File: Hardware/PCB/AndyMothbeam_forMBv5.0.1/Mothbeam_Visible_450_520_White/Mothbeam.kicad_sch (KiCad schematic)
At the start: 26 parts, among them CN1 X6511FRS-04-C85D30, SW2 SW_DIP_x04, U1 BCR421U, U2 BCR421U, U3 BCR421U, U4 M3535N1UVS8U12- 405NM, U5 M3535N1UVS8U06-385NM, U6 JNJ-LEHG0113W120/45MIL/525-53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

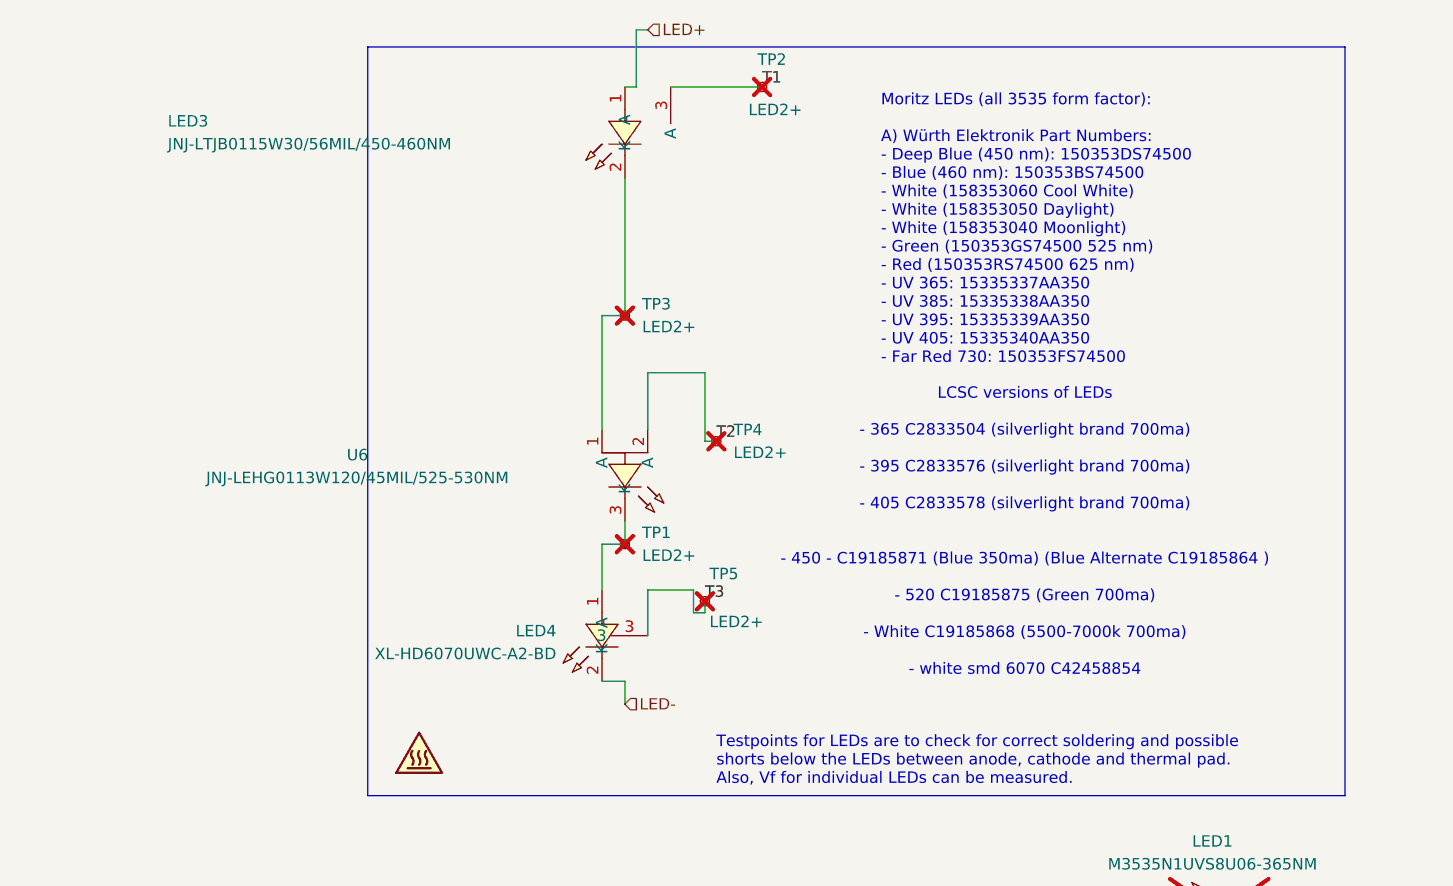
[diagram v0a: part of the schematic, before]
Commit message: Created 3535 Mothbeams for UV and V
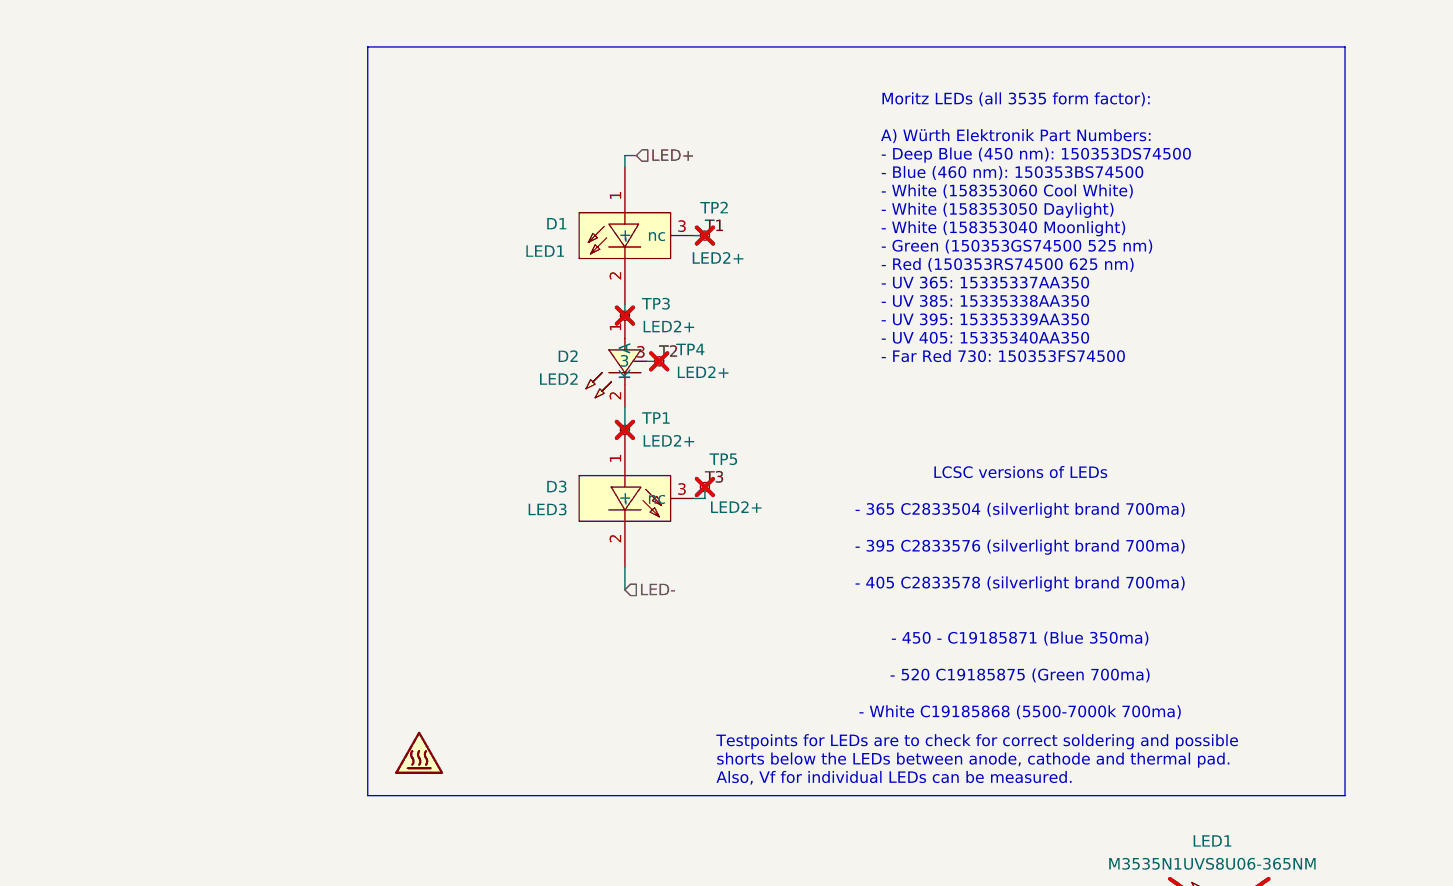
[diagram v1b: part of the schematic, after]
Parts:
- removed LED3: JNJ-LTJB0115W30/56MIL/450-460NM, easyeda2kicad:LED-SMD_3P-L3.5-W3.5-FD-1, symbol easyeda2kicad:JNJ-LTJB0115W30_56MIL_450-460NM
- removed LED4: XL-HD6070UWC-A2-BD, easyeda2kicad:LED-SMD_XL-HD6070UBC-A2, symbol easyeda2kicad:XL-HD6070UWC-A2-BD
- removed U6: JNJ-LEHG0113W120/45MIL/525-530NM, easyeda2kicad:LED-SMD_3P-L3.5-W3.5-R-RD_C9900043159, symbol easyeda2kicad:JNJ-LEHG0113W120_45MIL_525-530NM
- added D1: LED1, easyeda2kicad:LED-SMD_3P-L3.5-W3.5-R-RD-C, symbol easyeda2kicad:M3535N1UVS8U12-365NM
- added D2: LED2, easyeda2kicad:LED-SMD_3P-L3.5-W3.5-R-RD-C, symbol easyeda2kicad:M3535N1UVS8U12-395NM
- added D3: LED3, easyeda2kicad:LED-SMD_3P-L3.5-W3.5-R-RD-C, symbol easyeda2kicad:M3535N1UVS8U12-405NM
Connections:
- net LED+: now also D1.1 (+)
- net LED-: now also D3.2 (-)
- net T1: now also D1.3 (nc)
- net T2: now also D2.3
- net T3: now also D3.3 (nc)
- net at TP3.1: now also D1.2 (-), D2.1 (A)
- net at TP1.1: now also D2.2 (K), D3.1 (+)
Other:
- note added: "LCSC versions of LEDs - 365 C2833504 (silverlight brand 700ma) - 395 C2833576 (silverlight brand 700ma) - 405 C2833578 (silverlight brand 700ma) - 450 - C19185871 (Blue 350ma) - 520 C19185875 (Green 700ma) - White C19185868 (5500-7000k 700ma)"
- note removed: "LCSC versions of LEDs - 365 C2833504 (silverlight brand 700ma) - 395 C2833576 (silverlight brand 700ma) - 405 C2833578 (silverlight brand 700ma) - 450 - C19185871 (Blue 350ma) (Blue Alternate C19185864 ) - 520 C19185875 (Green 700ma) - White C19185868 (5500-7000k 700ma) - white smd 6070 C42458854"
- moved on the sheet: TP1, TP2, TP4, TP5

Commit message: before changing footprints on Visible board
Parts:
- removed D1: LED1, easyeda2kicad:LED-SMD_3P-L3.5-W3.5-R-RD-C, symbol easyeda2kicad:M3535N1UVS8U12-365NM
- removed D2: LED2, easyeda2kicad:LED-SMD_3P-L3.5-W3.5-R-RD-C, symbol easyeda2kicad:M3535N1UVS8U12-395NM
- removed D3: LED3, easyeda2kicad:LED-SMD_3P-L3.5-W3.5-R-RD-C, symbol easyeda2kicad:M3535N1UVS8U12-405NM
- added LED2: JNJ-LEJB0111W60/26MIL/450-460NM, easyeda2kicad:LED-SMD_3P-L3.5-W3.5_JNJ-LEJB0111W60, symbol easyeda2kicad:JNJ-LEJB0111W60_26MIL_450-460NM
- added LED3: JNJ-LEJW0113W30/C36MIL/5500-6500K, easyeda2kicad:LED-SMD_3P-L3.5-W3.5-R-RD-B, symbol easyeda2kicad:JNJ-LEJW0113W30_C36MIL_5500-6500K
- added U6: JNJ-LEHG0113W120/45MIL/525-530NM, easyeda2kicad:LED-SMD_3P-L3.5-W3.5-R-RD_C9900043159, symbol easyeda2kicad:JNJ-LEHG0113W120_45MIL_525-530NM
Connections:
- net LED+: now also LED2.3 (A)
- net LED-: now also LED3.3
- net T1: now also LED2.2 (K)
- net T2: now also U6.2 (A)
- net T3: now also LED3.2
- net at TP3.1: now also LED2.1 (K), U6.1 (A)
- net at TP1.1: now also LED3.1, U6.3 (K)
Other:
- moved on the sheet: TP1, TP2, TP4, TP5

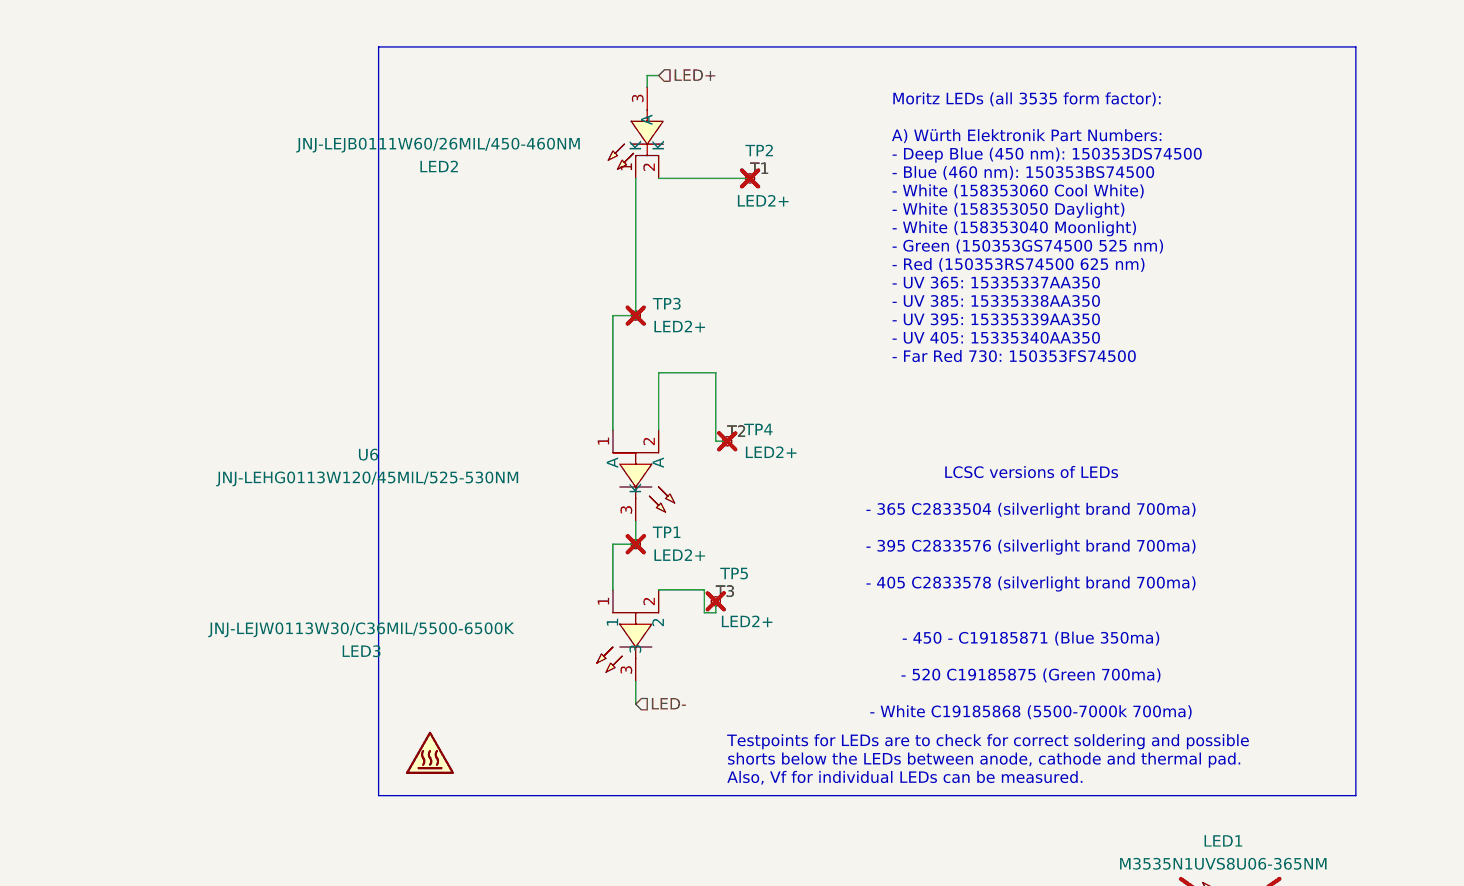
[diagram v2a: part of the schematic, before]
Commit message: new substitute parts
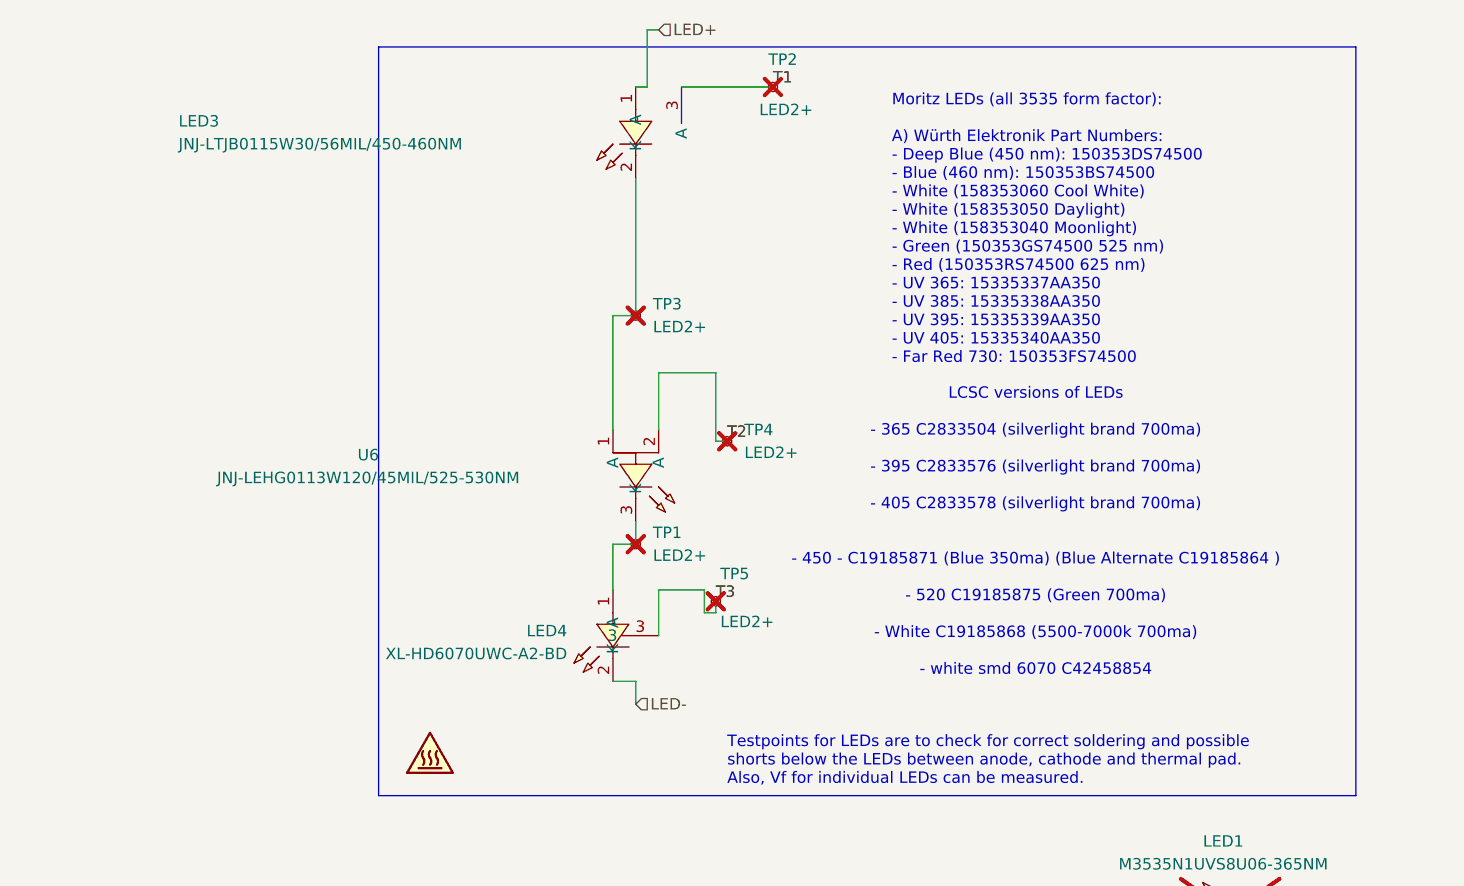
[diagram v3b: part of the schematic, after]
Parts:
- removed LED2: JNJ-LEJB0111W60/26MIL/450-460NM, easyeda2kicad:LED-SMD_3P-L3.5-W3.5_JNJ-LEJB0111W60, symbol easyeda2kicad:JNJ-LEJB0111W60_26MIL_450-460NM
- removed LED3: JNJ-LEJW0113W30/C36MIL/5500-6500K, easyeda2kicad:LED-SMD_3P-L3.5-W3.5-R-RD-B, symbol easyeda2kicad:JNJ-LEJW0113W30_C36MIL_5500-6500K
- added LED3: JNJ-LTJB0115W30/56MIL/450-460NM, easyeda2kicad:LED-SMD_3P-L3.5-W3.5-FD-1, symbol easyeda2kicad:JNJ-LTJB0115W30_56MIL_450-460NM
- added LED4: XL-HD6070UWC-A2-BD, easyeda2kicad:LED-SMD_XL-HD6070UBC-A2, symbol easyeda2kicad:XL-HD6070UWC-A2-BD
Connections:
- net LED+: now also LED3.1 (A)
- net LED-: now also LED4.2 (K)
- net T1: now also LED3.3 (A)
- net T3: now also LED4.3
- net at TP1.1, U6.3 (K): now also LED4.1 (A)
- net at TP3.1, U6.1 (A): now also LED3.2 (K)
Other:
- note added: "LCSC versions of LEDs - 365 C2833504 (silverlight brand 700ma) - 395 C2833576 (silverlight brand 700ma) - 405 C2833578 (silverlight brand 700ma) - 450 - C19185871 (Blue 350ma) (Blue Alternate C19185864 ) - 520 C19185875 (Green 700ma) - White C19185868 (5500-7000k 700ma) - white smd 6070 C42458854"
- note removed: "LCSC versions of LEDs - 365 C2833504 (silverlight brand 700ma) - 395 C2833576 (silverlight brand 700ma) - 405 C2833578 (silverlight brand 700ma) - 450 - C19185871 (Blue 350ma) - 520 C19185875 (Green 700ma) - White C19185868 (5500-7000k 700ma)"
- moved on the sheet: TP2
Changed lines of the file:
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@@
 		)
 	)
-	(text "LCSC versions of LEDs\n\n- 365 C2833504 (silverlight brand 700ma)\n\n- 395 C2833576 (silverlight brand 700ma)\n\n- 405 C2833578 (silverlight brand 700ma)\n\n\n- 450 - C19185871 (Blue 350ma)\n\n- 520 C19185875 (Green 700ma)\n\n- White C19185868 (5500-7000k 700ma)"
+	(text "LCSC versions of LEDs\n\n- 365 C2833504 (silverlight brand 700ma)\n\n- 395 C2833576 (silverlight brand 700ma)\n\n- 405 C2833578 (silverlight brand 700ma)\n\n\n- 450 - C19185871 (Blue 350ma) (Blue Alternate C19185864 )\n\n- 520 C19185875 (Green 700ma)\n\n- White C19185868 (5500-7000k 700ma)\n\n- white smd 6070 C42458854"
 		(exclude_from_sim no)
-		(at 245.872 76.708 0)
+		(at 246.38 69.85 0)
 		(effects
 			(font
@@
 	(wire
 		(pts
+			(xy 204.47 76.2) (xy 204.47 81.28)
+		)
+		(stroke
+			(width 0)
+			(type default)
+		)
+	)
+	(wire
+		(pts
 			(xy 45.72 134.62) (xy 48.26 134.62)
 		)
@@
 	(wire
 		(pts
+			(xy 203.2 13.97) (xy 203.2 20.32)
+		)
+		(stroke
+			(width 0)
+			(type default)
+		)
+	)
+	(wire
+		(pts
 			(xy 210.82 78.74) (xy 210.82 77.47)
 		)
@@
 	(wire
 		(pts
+			(xy 203.2 20.32) (xy 201.93 20.32)
+		)
+		(stroke
+			(width 0)
+			(type default)
+		)
+	)
+	(wire
+		(pts
 			(xy 201.93 30.48) (xy 201.93 45.72)
 		)
@@
 	(wire
 		(pts
+			(xy 199.39 86.36) (xy 201.93 86.36)
+		)
+		(stroke
+			(width 0)
+			(type default)
+		)
+	)
+	(wire
+		(pts
 			(xy 170.18 138.43) (xy 175.26 138.43)
 		)
@@
 	(wire
 		(pts
-			(xy 204.47 30.48) (xy 214.63 30.48)
+			(xy 207.01 20.32) (xy 217.17 20.32)
 		)
 		(stroke
@@
 	(wire
 		(pts
-			(xy 203.2 20.32) (xy 203.2 19.05)
-		)
-		(stroke
-			(width 0)
-			(type default)
-		)
-	)
-	(wire
-		(pts
 			(xy 41.91 134.62) (xy 41.91 127)
 		)
@@
 	(wire
 		(pts
-			(xy 203.2 19.05) (xy 204.47 19.05)
+			(xy 203.2 13.97) (xy 204.47 13.97)
 		)
 		(stroke
@@
 	)
 	(label "T1"
-		(at 214.63 30.48 0)
+		(at 217.17 20.32 0)
 		(effects
 			(font
@@
 	(hierarchical_label "LED+"
 		(shape input)
-		(at 204.47 19.05 0)
+		(at 204.47 13.97 0)
 		(effects
 			(font
@@
 	(symbol
 		(lib_id "Connector:TestPoint_Small")
-		(at 214.63 30.48 0)
+		(at 217.17 20.32 0)
 		(unit 1)
 		(exclude_from_sim no)
@@
 		(dnp yes)
 		(property "Reference" "TP2"
-			(at 214.122 27.432 0)
+			(at 216.662 17.272 0)
 			(effects
 				(font
@@
 		)
 		(property "Value" "LED2+"
-			(at 213.106 33.02 0)
+			(at 215.646 22.86 0)
 			(effects
 				(font
@@
 		)
 		(property "Footprint" "TestPoint:TestPoint_Pad_D1.5mm"
-			(at 219.71 30.48 0)
+			(at 222.25 20.32 0)
 			(effects
 				(font
@@
 		)
 		(property "Datasheet" "~"
-			(at 219.71 30.48 0)
+			(at 222.25 20.32 0)
 			(effects
 				(font
@@
 		)
 		(property "Description" ""
-			(at 214.63 30.48 0)
+			(at 217.17 20.32 0)
 			(effects
 				(font
@@
 	)
 	(symbol
-		(lib_id "easyeda2kicad:JNJ-LEJW0113W30_C36MIL_5500-6500K")
-		(at 201.93 81.28 90)
-		(unit 1)
-		(exclude_from_sim no)
-		(in_bom yes)
-		(on_board yes)
-		(dnp no)
-		(property "Reference" "LED3"
-			(at 171.45 83.058 90)
-			(effects
-				(font
-					(size 1.27 1.27)
-				)
-			)
-		)
-		(property "Value" "JNJ-LEJW0113W30/C36MIL/5500-6500K"
-			(at 171.45 80.518 90)
-			(effects
-				(font
-					(size 1.27 1.27)
-				)
-			)
-		)
-		(property "Footprint" "easyeda2kicad:LED-SMD_3P-L3.5-W3.5-R-RD-B"
-			(at 212.09 81.28 0)
-			(effects
-				(font
-					(size 1.27 1.27)
-				)
-				(hide yes)
-			)
-		)
-		(property "Datasheet" ""
-			(at 201.93 81.28 0)
-			(effects
-				(font
-					(size 1.27 1.27)
-				)
-				(hide yes)
-			)
-		)
-		(property "Description" ""
-			(at 201.93 81.28 0)
-			(effects
-				(font
-					(size 1.27 1.27)
-				)
-				(hide yes)
-			)
-		)
-		(property "LCSC Part" "C19185868"
-			(at 214.63 81.28 0)
-			(effects
-				(font
-					(size 1.27 1.27)
-				)
-				(hide yes)
-			)
-		)
-		(pin "1"
-		)
-		(pin "3"
-		)
-		(pin "2"
-		)
-		(instances
-			(project ""
-				(path "/a270892a-30ca-43aa-91d1-ed114756b159"
-					(reference "LED3")
-					(unit 1)
-				)
-			)
-		)
-	)
-	(symbol
 		(lib_id "Mechanical:Fiducial")
 		(at 27.94 183.515 0)
@@
 	)
 	(symbol
-		(lib_id "easyeda2kicad:JNJ-LEJB0111W60_26MIL_450-460NM")
-		(at 203.2 25.4 90)
-		(unit 1)
-		(exclude_from_sim no)
-		(in_bom yes)
-		(on_board yes)
-		(dnp no)
-		(property "Reference" "LED2"
-			(at 180.086 29.21 90)
-			(effects
-				(font
-					(size 1.27 1.27)
-				)
-			)
-		)
-		(property "Value" "JNJ-LEJB0111W60/26MIL/450-460NM"
-			(at 180.086 26.67 90)
-			(effects
-				(font
-					(size 1.27 1.27)
-				)
-			)
-		)
-		(property "Footprint" "easyeda2kicad:LED-SMD_3P-L3.5-W3.5_JNJ-LEJB0111W60"
-			(at 212.09 25.4 0)
-			(effects
-				(font
-					(size 1.27 1.27)
-				)
-				(hide yes)
-			)
-		)
-		(property "Datasheet" ""
-			(at 203.2 25.4 0)
-			(effects
-				(font
-					(size 1.27 1.27)
-				)
-				(hide yes)
-			)
-		)
-		(property "Description" ""
-			(at 203.2 25.4 0)
-			(effects
-				(font
-					(size 1.27 1.27)
-				)
-				(hide yes)
-			)
-		)
-		(property "LCSC Part" "C19185871"
-			(at 214.63 25.4 0)
-			(effects
-				(font
-					(size 1.27 1.27)
-				)
-				(hide yes)
-			)
-		)
-		(pin "2"
-		)
-		(pin "1"
-		)
-		(pin "3"
-		)
-		(instances
-			(project ""
-				(path "/a270892a-30ca-43aa-91d1-ed114756b159"
-					(reference "LED2")
-					(unit 1)
-				)
-			)
-		)
-	)
-	(symbol
 		(lib_id "easyeda2kicad:BCR421UW6-7")
 		(at 60.96 134.62 180)
@@
 	)
 	(symbol
+		(lib_id "easyeda2kicad:XL-HD6070UWC-A2-BD")
+		(at 199.39 81.28 90)
+		(unit 1)
+		(exclude_from_sim no)
+		(in_bom yes)
+		(on_board yes)
+		(dnp no)
+		(fields_autoplaced yes)
+		(property "Reference" "LED4"
+			(at 194.31 80.7699 90)
+			(effects
+				(font
+					(size 1.27 1.27)
+				)
+				(justify left)
+			)
+		)
+		(property "Value" "XL-HD6070UWC-A2-BD"
+			(at 194.31 83.3099 90)
+			(effects
+				(font
+					(size 1.27 1.27)
+				)
+				(justify left)
+			)
+		)
+		(property "Footprint" "easyeda2kicad:LED-SMD_XL-HD6070UBC-A2"
+			(at 212.09 81.28 0)
+			(effects
+				(font
+					(size 1.27 1.27)
+				)
+				(hide yes)
+			)
+		)
+		(property "Datasheet" ""
+			(at 199.39 81.28 0)
+			(effects
+				(font
+					(size 1.27 1.27)
+				)
+				(hide yes)
+			)
+		)
+		(property "Description" ""
+			(at 199.39 81.28 0)
+			(effects
+				(font
+					(size 1.27 1.27)
+				)
+				(hide yes)
+			)
+		)
+		(property "LCSC Part" "C42458854"
+			(at 214.63 81.28 0)
+			(effects
+				(font
+					(size 1.27 1.27)
+				)
+				(hide yes)
+			)
+		)
+		(pin "3"
+		)
+		(pin "1"
+		)
+		(pin "2"
+		)
+		(instances
+			(project ""
+				(path "/a270892a-30ca-43aa-91d1-ed114756b159"
+					(reference "LED4")
+					(unit 1)
+				)
+			)
+		)
+	)
+	(symbol
 		(lib_id "Device:R")
 		(at 45.72 143.51 0)
@@
 					(unit 1)
 				)
+			)
+		)
+	)
+	(symbol
+		(lib_id "easyeda2kicad:JNJ-LTJB0115W30_56MIL_450-460NM")
+		(at 201.93 25.4 90)
+		(unit 1)
+		(exclude_from_sim no)
+		(in_bom yes)
+		(on_board yes)
+		(dnp no)
+		(property "Reference" "LED3"
+			(at 151.13 24.13 90)
+			(effects
+				(font
+					(size 1.27 1.27)
+				)
+				(justify right)
+			)
+		)
+		(property "Value" "JNJ-LTJB0115W30/56MIL/450-460NM"
+			(at 151.13 26.67 90)
+			(effects
+				(font
+					(size 1.27 1.27)
+				)
+				(justify right)
+			)
+		)
+		(property "Footprint" "easyeda2kicad:LED-SMD_3P-L3.5-W3.5-FD-1"
+			(at 214.63 25.4 0)
+			(effects
+				(font
+					(size 1.27 1.27)
+				)
+				(hide yes)
+			)
+		)
+		(property "Datasheet" ""
+			(at 201.93 25.4 0)
+			(effects
+				(font
+					(size 1.27 1.27)
+				)
+				(hide yes)
+			)
+		)
+		(property "Description" ""
+			(at 201.93 25.4 0)
+			(effects
+				(font
+					(size 1.27 1.27)
+				)
+				(hide yes)
+			)
+		)
+		(property "LCSC Part" "C19185864"
+			(at 217.17 25.4 0)
+			(effects
+				(font
+					(size 1.27 1.27)
+				)
+				(hide yes)
+			)
+		)
+		(pin "3"
+		)
+		(pin "2"
+		)
+		(pin "1"
+		)
+		(instances
+			(project ""
+				(path "/a270892a-30ca-43aa-91d1-ed114756b159"
+					(reference "LED3")
+					(unit 1)
+				)
